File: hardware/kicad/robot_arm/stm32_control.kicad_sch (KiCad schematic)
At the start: 0 parts

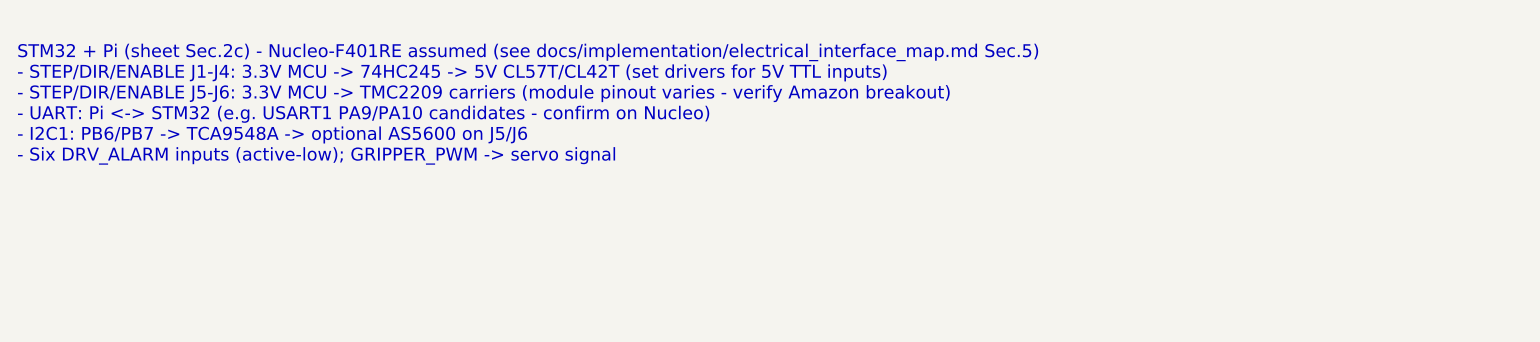
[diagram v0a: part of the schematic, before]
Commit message: docs: Update documentation and schematics to reflect transition from Raspberry Pi 3 to Raspberry Pi 4 for high-level control and power management. Adjusted references in README, calculations, design choices, examples, scope, and electrical schematics. Enhanced BOM and electrical interface documentation for improved clarity on power requirements and connections.
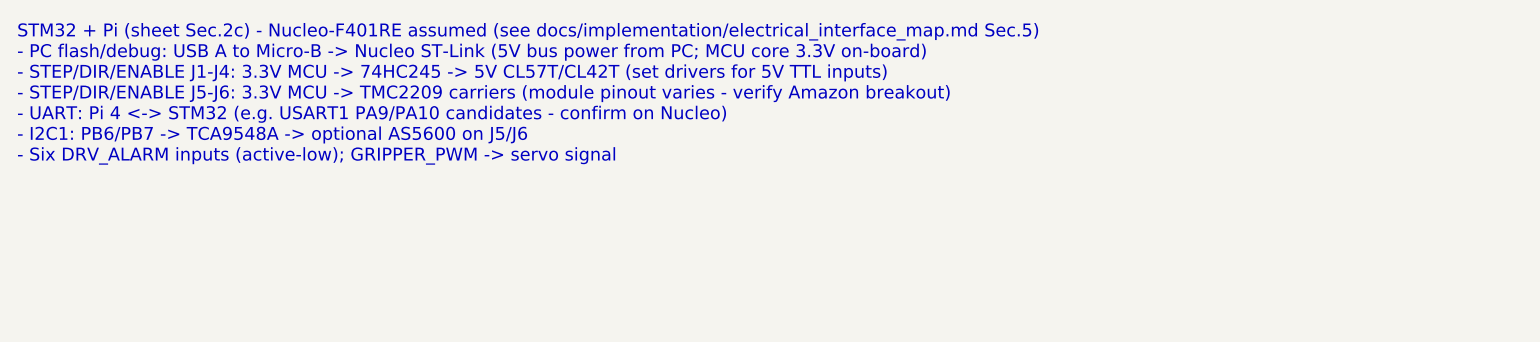
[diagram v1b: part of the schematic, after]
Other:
- note added: "STM32 + Pi (sheet Sec.2c) - Nucleo-F401RE assumed (see docs/implementation/electrical_interface_map.md Sec.5) - PC flash/debug: USB A to Micro-B -> Nucleo ST-Link (5V bus power from PC; MCU core 3.3V on-board) - STEP/DIR/ENABLE J1-J4: 3.3V MCU -> 74HC245 -> 5V CL57T/CL42T (set drivers for 5V TTL inputs) - STEP/DIR/ENABLE J5-J6: 3.3V MCU -> TMC2209 carriers (module pinout varies - verify Amazon br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"
- note removed: "STM32 + Pi (sheet Sec.2c) - Nucleo-F401RE assumed (see docs/implementation/electrical_interface_map.md Sec.5) - STEP/DIR/ENABLE J1-J4: 3.3V MCU -> 74HC245 -> 5V CL57T/CL42T (set drivers for 5V TTL inputs) - STEP/DIR/ENABLE J5-J6: 3.3V MCU -> TMC2209 carriers (module pinout varies - verify Amazon breakout) - UART: Pi <-> STM32 (e.g. USART1 PA9/PA10 candidates - confirm on Nucleo) - I2C1: PB6/PB7 -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"
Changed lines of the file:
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@@
 		(rev "0.1")
 	)
-	(text "STM32 + Pi (sheet Sec.2c) - Nucleo-F401RE assumed (see docs/implementation/electrical_interface_map.md Sec.5)\n- STEP/DIR/ENABLE J1-J4: 3.3V MCU -> 74HC245 -> 5V CL57T/CL42T (set drivers for 5V TTL inputs)\n- STEP/DIR/ENABLE J5-J6: 3.3V MCU -> TMC2209 carriers (module pinout varies - verify Amazon breakout)\n- UART: Pi <-> STM32 (e.g. USART1 PA9/PA10 candidates - confirm on Nucleo)\n- I2C1: PB6/PB7 -> TCA9548A -> optional AS5600 on J5/J6\n- Six DRV_ALARM inputs (active-low); GRIPPER_PWM -> servo signal"
+	(text "STM32 + Pi (sheet Sec.2c) - Nucleo-F401RE assumed (see docs/implementation/electrical_interface_map.md Sec.5)\n- PC flash/debug: USB A to Micro-B -> Nucleo ST-Link (5V bus power from PC; MCU core 3.3V on-board)\n- STEP/DIR/ENABLE J1-J4: 3.3V MCU -> 74HC245 -> 5V CL57T/CL42T (set drivers for 5V TTL inputs)\n- STEP/DIR/ENABLE J5-J6: 3.3V MCU -> TMC2209 carriers (module pinout varies - verify Amazon breakout)\n- UART: Pi 4 <-> STM32 (e.g. USART1 PA9/PA10 candidates - confirm on Nucleo)\n- I2C1: PB6/PB7 -> TCA9548A -> optional AS5600 on J5/J6\n- Six DRV_ALARM inputs (active-low); GRIPPER_PWM -> servo signal"
 		(exclude_from_sim no)
 		(at 12 12 0)
